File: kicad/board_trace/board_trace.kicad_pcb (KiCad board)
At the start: 2 copper layers, 39.7 x 61.7 mm, 43 parts, among them J3 C42418480_CONN-SMD_20P-P0_80_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, U1 C69418_QFN-76_L9_0-W9_0-P0_40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, Y1 Crystal_SMD_3225-4Pin_3.2x2.5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

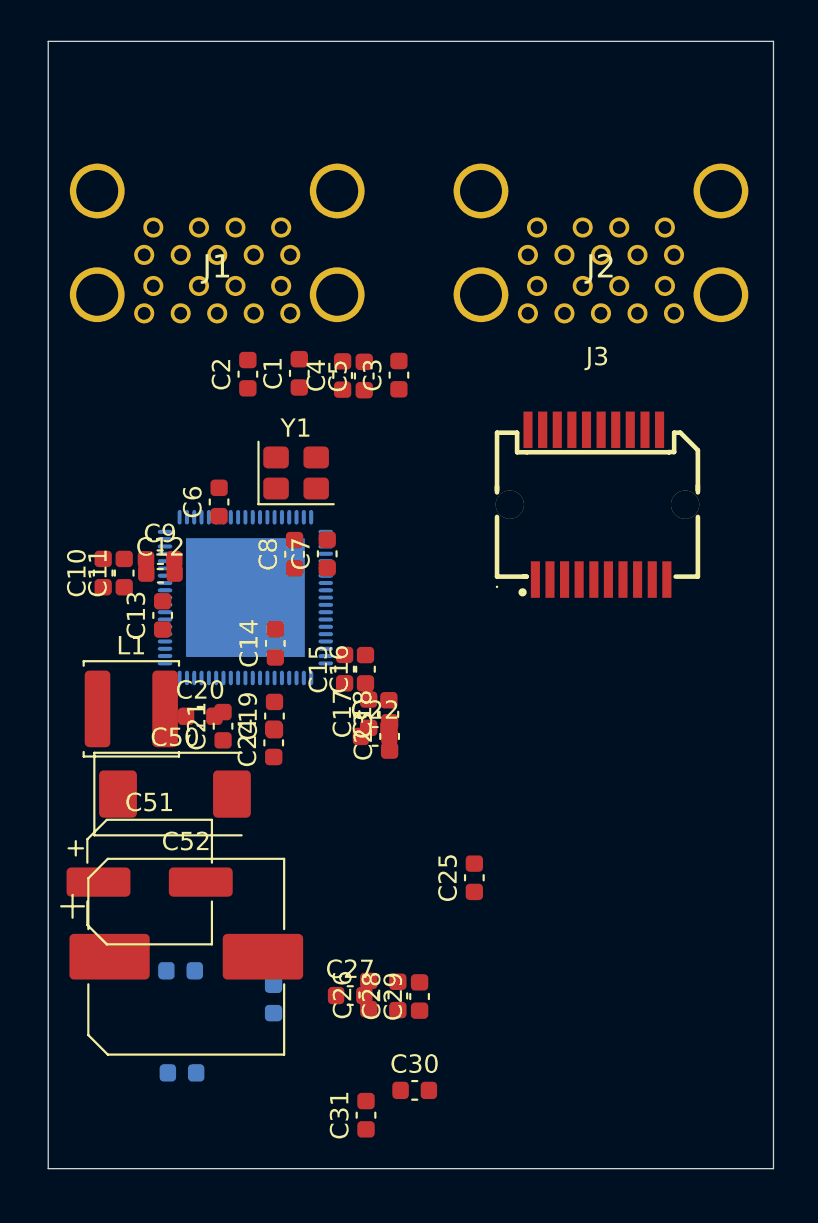
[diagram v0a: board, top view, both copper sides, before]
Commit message: Refine board_trace photo placement model and verification
Fit J1/J2 to all 22 visible joints per bottom photo (RMS 0.075/0.072 mm, max 0.216/0.161 mm photo-fit error). Replace per-pad detections with manually reviewed component centers in scripts/04_review_plan.py and record retired references and rationale in placement_plan.json.

Reclassify discovered parts: C52 -> J4 traced barrel jack, C32-C34 -> jack tabs, C51 -> radial through-hole electrolytic, C50 -> provisional D1, plus added MLCCs, R1-R11, L2/L3, U2 and D2/D3. All nonstandard footprints are now local with an fp-lib-table; board and footprint writes use the native pcbnew API only.

Add scripts 04_review_plan.py, 05_overlay.py and 06_check_saved.py, regenerated Edge.Cuts/overlays and PLACEMENT_REVIEW.md. Structural checks pass; native DRC still reports 112 errors/175 warnings and is not a fabrication pass.
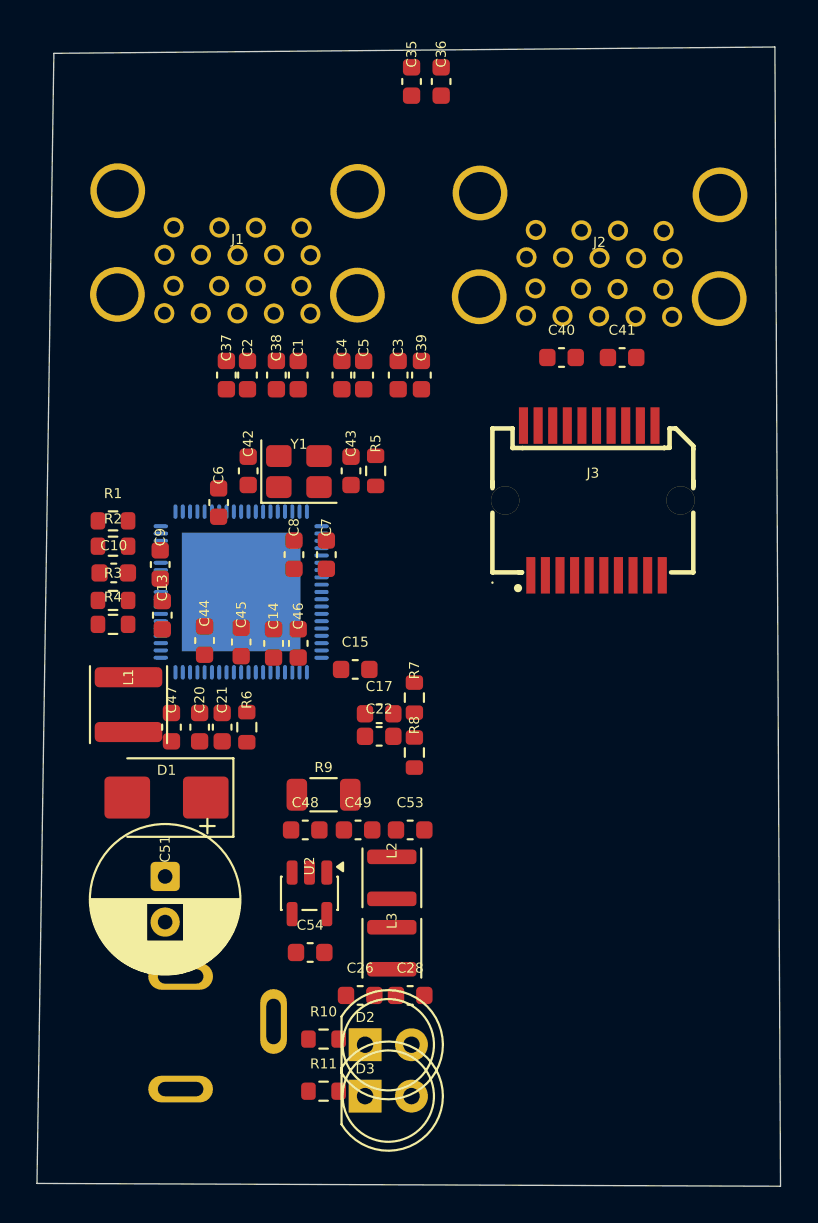
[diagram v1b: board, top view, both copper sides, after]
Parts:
- removed C11, C12, C16, C18, C19, C23, C24, C25, C27, C29, C30, C31, C32, C33, C34: C_0603_1608Metric, C_0603_1608Metric
- removed C50: CP_EIA-7343-30_AVX-N, CP_EIA-7343-30_AVX-N
- removed C52: CP_Elec_10x10.5, CP_Elec_10x10.5
- added C35: UNKNOWN, Capacitor_SMD:C_0603_1608Metric, F.Cu at (148.5, 76.3)
- added C36: UNKNOWN, Capacitor_SMD:C_0603_1608Metric, F.Cu at (150.2, 76.3)
- added C37: UNKNOWN, Capacitor_SMD:C_0603_1608Metric, F.Cu at (138.4, 92.4)
- added C38: UNKNOWN, Capacitor_SMD:C_0603_1608Metric, F.Cu at (141.1, 92.4)
- added C39: UNKNOWN, Capacitor_SMD:C_0603_1608Metric, F.Cu at (149.1, 92.4)
- added C40: UNKNOWN, Capacitor_SMD:C_0603_1608Metric, F.Cu at (156.8, 91.4)
- added C41: UNKNOWN, Capacitor_SMD:C_0603_1608Metric, F.Cu at (160.1, 91.4)
- added C42: UNKNOWN, Capacitor_SMD:C_0603_1608Metric, F.Cu at (139.6, 97.7)
- added C43: UNKNOWN, Capacitor_SMD:C_0603_1608Metric, F.Cu at (145.2, 97.7)
- added C44: UNKNOWN, Capacitor_SMD:C_0603_1608Metric, F.Cu at (137.2, 106.9)
- added C45: UNKNOWN, Capacitor_SMD:C_0603_1608Metric, F.Cu at (139.2, 107.0)
- added C46: UNKNOWN, Capacitor_SMD:C_0603_1608Metric, F.Cu at (142.3, 107.1)
- added C47: UNKNOWN, Capacitor_SMD:C_0603_1608Metric, F.Cu at (135.4, 111.7)
- added C48: UNKNOWN, Capacitor_SMD:C_0603_1608Metric, F.Cu at (142.7, 117.3)
- added C49: UNKNOWN, Capacitor_SMD:C_0603_1608Metric, F.Cu at (145.6, 117.3)
- added C53: UNKNOWN, Capacitor_SMD:C_0603_1608Metric, F.Cu at (148.5, 117.3)
- added C54: UNKNOWN, Capacitor_SMD:C_0603_1608Metric, F.Cu at (143.0, 124.0)
- added D1: UNKNOWN (MARK:KE), Diode_SMD:D_SMB, F.Cu at (135.1, 115.5)
- added D2: LED (bent leads), LED_THT:LED_D5.0mm, F.Cu at (146.0, 129.1)
- added D3: LED (bent leads), LED_THT:LED_D5.0mm, F.Cu at (146.0, 131.9)
- added J4: DC barrel jack (unidentified), trace:BarrelJack_PhotoTrace, F.Cu at (136.0, 125.3)
- added L2: UNKNOWN, Inductor_SMD:L_Sunlord_SWPA3015S, F.Cu at (147.5, 119.9)
- added L3: UNKNOWN, Inductor_SMD:L_Sunlord_SWPA3015S, F.Cu at (147.5, 123.8)
- added R1: MARK:472, Resistor_SMD:R_0603_1608Metric, F.Cu at (132.2, 100.4)
- added R10: MARK:331, Resistor_SMD:R_0603_1608Metric, F.Cu at (143.7, 128.8)
- added R11: MARK:331, Resistor_SMD:R_0603_1608Metric, F.Cu at (143.7, 131.6)
- added R2: MARK:472, Resistor_SMD:R_0603_1608Metric, F.Cu at (132.2, 101.8)
- added R3: MARK:473, Resistor_SMD:R_0603_1608Metric, F.Cu at (132.2, 104.7)
- added R4: MARK:472, Resistor_SMD:R_0603_1608Metric, F.Cu at (132.2, 106.1)
- added R5: MARK:68?, Resistor_SMD:R_0603_1608Metric, F.Cu at (146.6, 97.7)
- added R6: MARK:472, Resistor_SMD:R_0603_1608Metric, F.Cu at (139.5, 111.7)
- added R7: MARK:331, Resistor_SMD:R_0603_1608Metric, F.Cu at (148.7, 110.1)
- added R8: MARK:331, Resistor_SMD:R_0603_1608Metric, F.Cu at (148.7, 113.1)
- added R9: MARK:1R0, Resistor_SMD:R_1206_3216Metric, F.Cu at (143.7, 115.4)
- added U2: UNKNOWN, Package_TO_SOT_SMD:SOT-23-5, F.Cu at (142.9, 120.8)
- C1, C10, C13, C14, C15, C17, C2, C20, C21, C22, C26, C28, C3, C4, C5, C6, C7, C8, C9: value C_0603_1608Metric -> UNKNOWN; footprint C_0603_1608Metric -> Capacitor_SMD:C_0603_1608Metric
- C51: value CP_Elec_6.3x5.4 -> UNKNOWN; footprint CP_Elec_6.3x5.4 -> Capacitor_THT:CP_Radial_D8.0mm_P2.50mm
- J1, J2: value (none) -> USB3 stacked Type-A (candidate); footprint HC-USB3.0-L175-2X1-P -> lcsc:HC-USB3.0-L175-2X1-P
- J3: value C42418480_CONN-SMD_20P-P0_80_SFP20P -> SFP20 (candidate); footprint C42418480_CONN-SMD_20P-P0_80_SFP20P -> lcsc:C42418480_CONN-SMD_20P-P0_80_SFP20P
- L1: value L_Sunlord_SWPA5040S -> 10uH; footprint L_Sunlord_SWPA5040S -> Inductor_SMD:L_Sunlord_SWPA4030S
- U1: value C69418_QFN-76_L9_0-W9_0-P0_40-EP6_4-TL -> VL813 (candidate); footprint C69418_QFN-76_L9_0-W9_0-P0_40-EP6_4-TL -> lcsc:C69418_QFN-76_L9_0-W9_0-P0_40-EP6_4-TL
- Y1: value Crystal_SMD_3225-4Pin_3.2x2.5mm -> 25MHz; footprint Crystal_SMD_3225-4Pin_3.2x2.5mm -> Crystal:Crystal_SMD_3225-4Pin_3.2x2.5mm
- moved J1 1.11 mm to (139.0, 86.5), turned to -0.169414 degrees
- moved C51 0.90 mm to (135.0, 119.9), turned to -90 degrees
- moved C28 0.67 mm to (148.5, 126.4), turned to 0 degrees
- moved C20 0.60 mm to (136.9, 111.7), turned to 90 degrees
- moved C15 0.58 mm to (145.5, 108.5), turned to 0 degrees
- moved C10 0.58 mm to (132.2, 103.2), turned to 0 degrees
- moved C17 0.57 mm to (146.8, 111.0), turned to 0 degrees
- moved C26 0.48 mm to (145.7, 126.4), turned to 0 degrees
- moved U1 0.39 mm to (139.2, 104.3)
- moved J3 0.34 mm to (158.5, 99.3)
- moved L1 0.28 mm to (133.0, 110.5), turned to 90 degrees
- moved C9 0.26 mm to (134.8, 102.8), turned to 90 degrees
- moved C22 0.22 mm to (146.8, 112.2)
- moved J2 0.18 mm to (158.8, 86.6), turned to -0.442564 degrees
- moved Y1 0.17 mm to (142.4, 97.7)
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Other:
- board size 39.7 x 61.7 mm -> 40.7 x 62.4 mm
